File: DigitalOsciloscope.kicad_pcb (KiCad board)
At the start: 4 copper layers, 150 x 150 mm, 413 parts, among them J1 Conn_Coaxial, J10 Conn_01x02_Pin, J11 Screw_Terminal_01x02, J12 Screw_Terminal_01x03, J2 Conn_Coaxial, J3 Conn_Coaxial, J4 Conn_01x03_Pin, J5 Conn_01x03_Pin, J6 Conn_01x02_Pin, J7 Conn_01x03_Pin, J8 Conn_01x02_Pin, J9 Conn_01x02_Pin, K1 TQ2-5V, K2 TQ2-5V, K3 TQ2-5V, K4 TQ2-5V, K5 TQ2-5V, K6 TQ2-5V, K7 TQ2-5V, Q1 2N7002, Q2 2N7002, Q3 2N7002, Q4 2N7002, Q5 2N7002, Q6 2N7002, Q7 2N7002, U1 TL072, U10 P0082_BOTTOMMOUNT, U11 NUCLEOH723ZG, U13 AZ1117-ADJ, U14 AZ1117-ADJ, U15 AZ1117-ADJ, U16 AZ1117-ADJ, U17 ADP7182AUJZ, U18 ADP7182AUJZ, U19 AZ1117-ADJ, U2 OPA656U, U20 DAC61408RHAR, U3 OPA656U, U4 AD8611ARZ, U5 AD8337BCPZ-REEL-ND, U6 AD8337BCPZ-REEL-ND, U7 AD8138ARZ, U8 AD8138ARZ, U9 LTC2299xUP, Y1 XLL735080.000000I

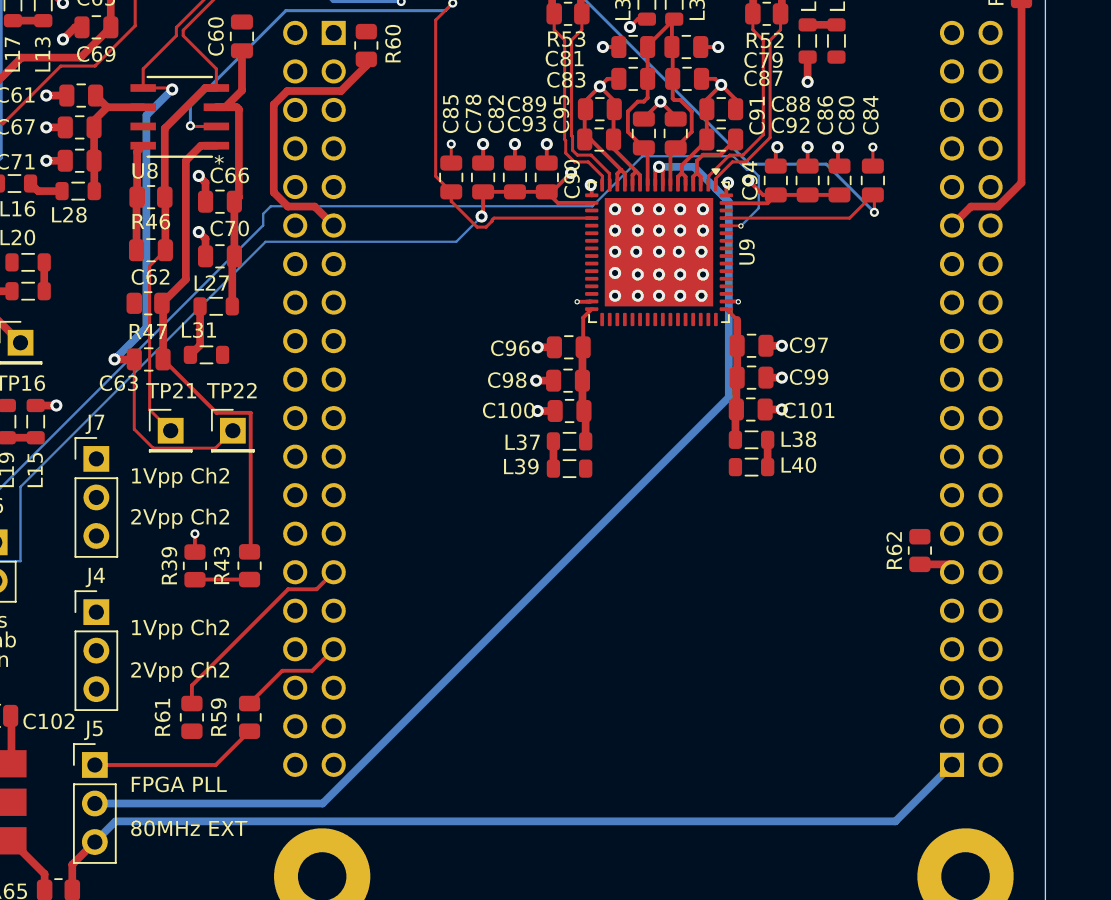
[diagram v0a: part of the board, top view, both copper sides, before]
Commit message: Done routing FGPA ADC data lines
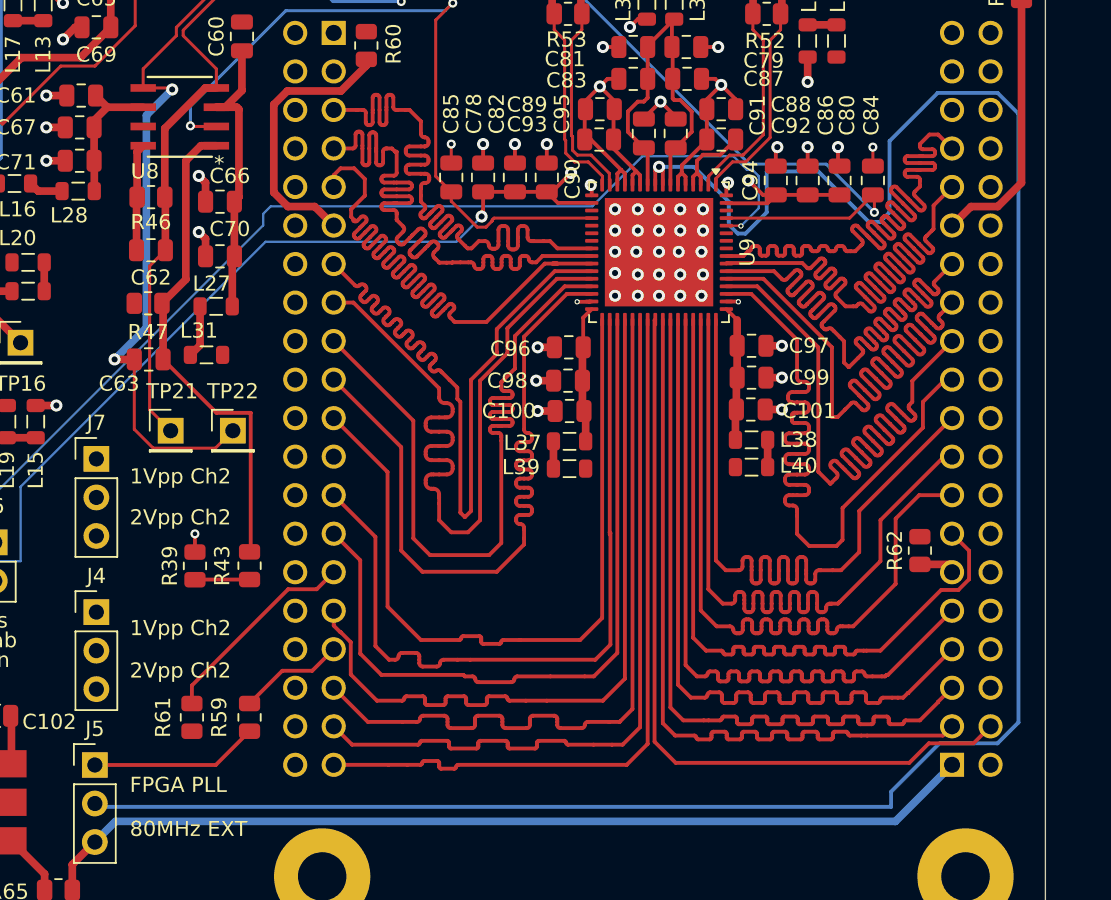
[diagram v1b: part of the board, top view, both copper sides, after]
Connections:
- U10 pad JP2_13: ADC_A_9 -> ADC_A_4
- U10 pad JP2_15: ADC_A_8 -> ADC_A_5
- U10 pad JP2_17: ADC_A_7 -> ADC_A_6
- U10 pad JP2_19: ADC_A_6 -> ADC_A_7
- U10 pad JP2_21: ADC_A_5 -> ADC_A_8
- U10 pad JP2_23: ADC_A_4 -> ADC_A_9
- U10 pad JP2_25: ADC_A_3 -> ADC_A_10
- U10 pad JP2_27: ADC_A_2 -> ADC_A_11
- U10 pad JP2_3: ADC_A_13 -> ADC_A_0
- U10 pad JP2_31: unconnected-(U10B-GPIO_124-PadJP2_31) -> ADC_A_12
- U10 pad JP2_33: ADC_A_1 -> ADC_A_13
- U10 pad JP2_35: ADC_A_0 -> unconnected-(U10B-GPIO_128-PadJP2_35)
- U10 pad JP2_5: ADC_A_12 -> ADC_A_1
- U10 pad JP2_7: ADC_A_11 -> ADC_A_2
- U10 pad JP2_9: ADC_A_10 -> ADC_A_3
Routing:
- net Net-(J5-Pin_2): track 73.9 -> 144.5 mm
- net CLIPPING: track 0.00 -> 51.6 mm
- net ADC_A_6: track 0.00 -> 50.8 mm
- net ADC_A_10: track 0.00 -> 50.6 mm
- net ADC_A_8: track 0.00 -> 50.5 mm
- net ADC_B_3: track 0.00 -> 50.4 mm
- net ADC_B_2: track 0.00 -> 50.3 mm
- net ADC_B_11: track 0.00 -> 50.2 mm
- net ADC_B_8: track 0.00 -> 50.1 mm
- net ADC_A_2: track 0.00 -> 50.1 mm
- net ADC_A_0: track 0.00 -> 50.0 mm
- net ADC_A_1: track 0.00 -> 50.0 mm
- net ADC_B_13: track 0.00 -> 49.9 mm
- net ADC_A_9: track 0.00 -> 49.9 mm
- net ADC_B_7: track 0.00 -> 49.9 mm
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
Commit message: Finish 5V_EXT?
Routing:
- net +5V_EXT: track 34.6 -> 481.7 mm, vias 4 -> 21
- net +5V: track 55.1 -> 85.7 mm
- net +6V5: track 55.1 -> 74.4 mm
- net +3V3DRV: vias 1 -> 7
- added copper zone on In1.Cu, net +3V3DRV
- added copper zone on In1.Cu, net +5V_EXT

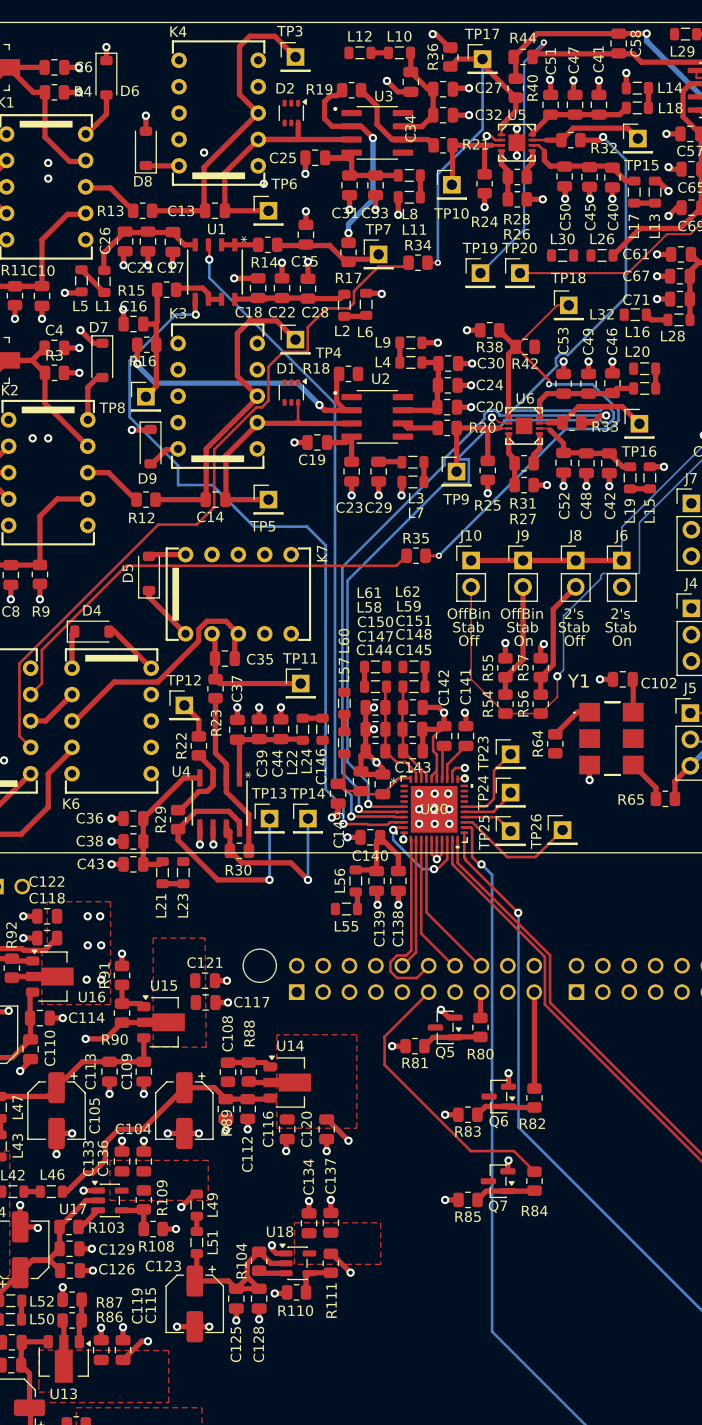
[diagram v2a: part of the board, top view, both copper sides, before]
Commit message: Route +5V and -5V
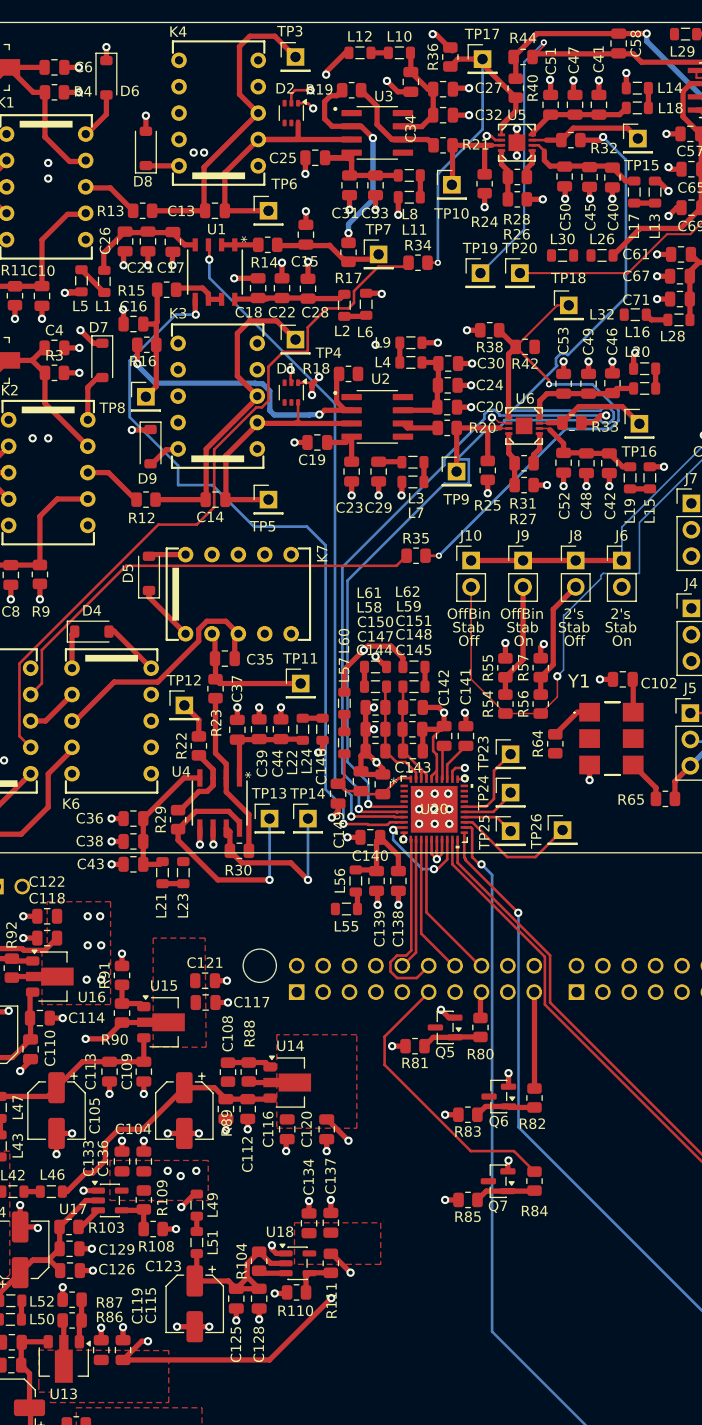
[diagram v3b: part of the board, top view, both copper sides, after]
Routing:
- net -5V: track 52.1 -> 300.1 mm, vias 7 -> 14
- net +5V: track 85.7 -> 313.4 mm, vias 5 -> 13
- net Net-(U2-NEG): track 28.9 -> 30.4 mm
- net +5V_EXT: track 481.7 -> 480.8 mm
- added copper zone on In1.Cu, net +5V
- added copper zone on In1.Cu, net -5V
